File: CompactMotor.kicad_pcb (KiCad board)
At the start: 4 copper layers, 39.4 x 41.3 mm, 29 parts, among them J1 Conn_01x04_Male, U2 AMS1117-3.3

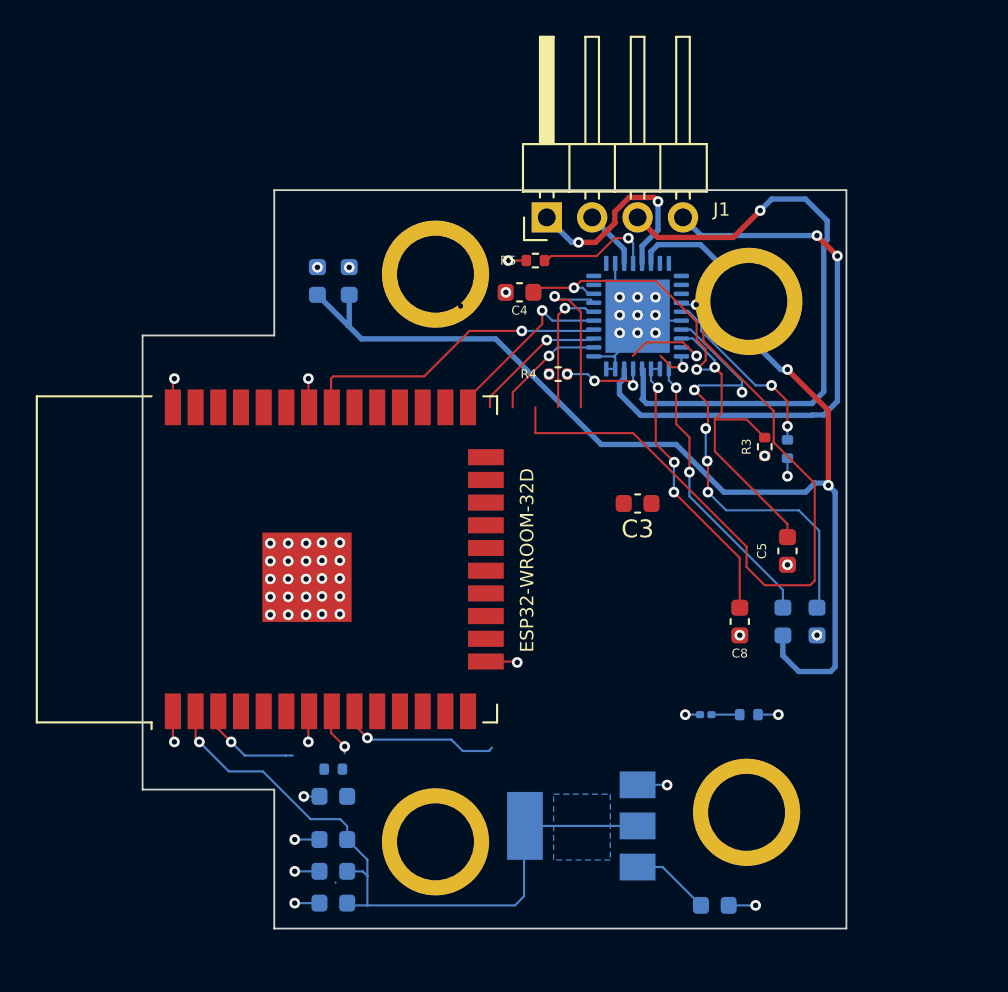
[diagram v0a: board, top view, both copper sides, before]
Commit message: Only trx-rx
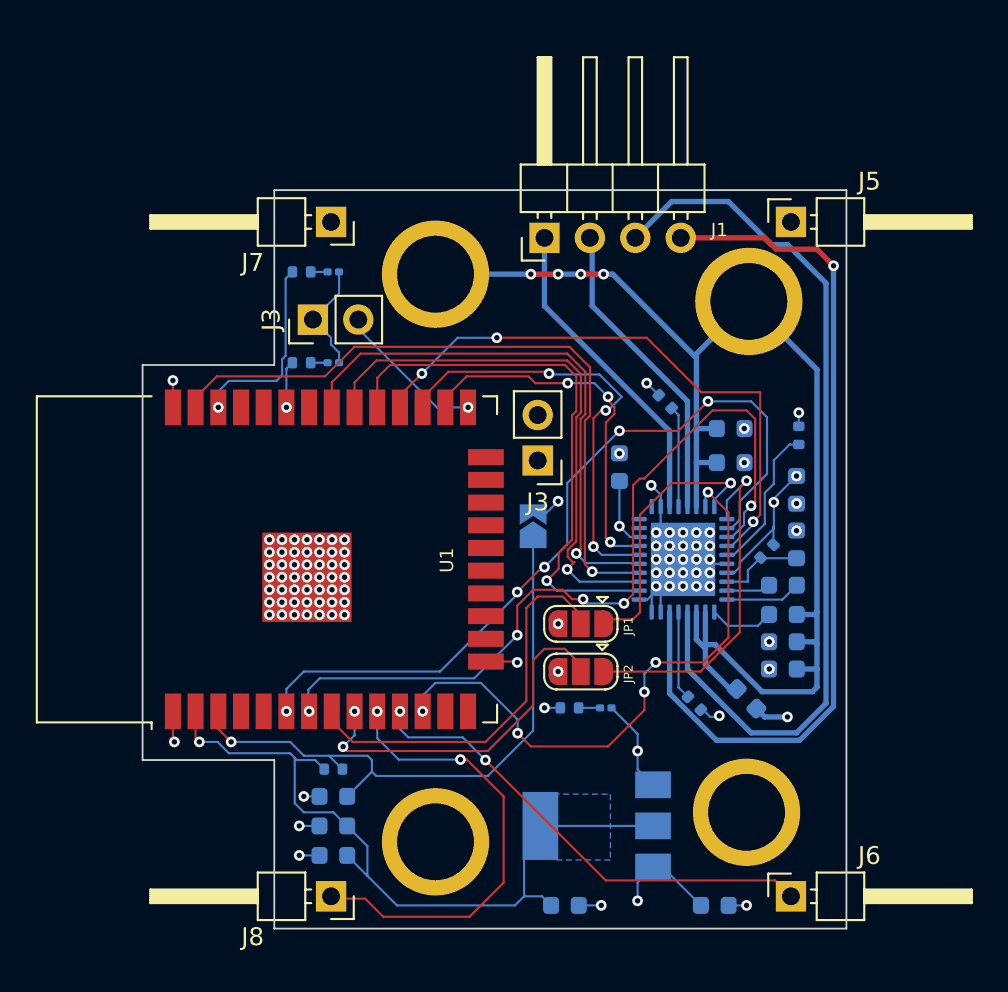
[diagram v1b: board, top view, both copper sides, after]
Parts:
- added C14: C100nF, Capacitor_SMD:C_0603_1608Metric, B.Cu at (28.4, 25.3)
- added C15: C1uF, Capacitor_SMD:C_0603_1608Metric, B.Cu at (28.4, 26.8)
- added D2: LED, LED_SMD:LED_0201_0603Metric, B.Cu at (3.30, 9.65)
- added D3: LED, LED_SMD:LED_0201_0603Metric, B.Cu at (3.30, 4.57)
- added J3: Conn_01x02_Female, Connector_PinHeader_2.54mm:PinHeader_1x02_P2.54mm_Vertical, F.Cu at (14.7, 15.1)
- added J3: Conn_01x02_Female, Connector_PinHeader_2.54mm:PinHeader_1x02_P2.54mm_Vertical, F.Cu at (2.16, 7.24)
- added J5: Conn_01x01_Male, Connector_PinHeader_2.54mm:PinHeader_1x01_P2.54mm_Horizontal, F.Cu at (28.9, 1.78)
- added J6: Conn_01x01_Male, Connector_PinHeader_2.54mm:PinHeader_1x01_P2.54mm_Horizontal, F.Cu at (28.9, 39.5)
- added J7: Conn_01x01_Male, Connector_PinHeader_2.54mm:PinHeader_1x01_P2.54mm_Horizontal, F.Cu at (3.17, 1.78)
- added J8: Conn_01x01_Male, Connector_PinHeader_2.54mm:PinHeader_1x01_P2.54mm_Horizontal, F.Cu at (3.17, 39.5)
- added JP1: SolderJumper_3_Open, Jumper:SolderJumper-3_P1.3mm_Open_RoundedPad1.0x1.5mm, F.Cu at (17.1, 24.3)
- added JP2: SolderJumper_3_Open, Jumper:SolderJumper-3_P1.3mm_Open_RoundedPad1.0x1.5mm, F.Cu at (17.1, 26.9)
- added JP3: SolderJumper_2_Open, Jumper:SolderJumper-2_P1.3mm_Open_TrianglePad1.0x1.5mm, B.Cu at (14.5, 18.8)
- added R7: R2k, Resistor_SMD:R_0402_1005Metric, B.Cu at (1.52, 9.65)
- added R8: R2k, Resistor_SMD:R_0402_1005Metric, B.Cu at (1.53, 4.57)
- C3, C4, C5, C8, R3, R4, R5: moved to B.Cu
- moved C13 24.5 mm to (25.5, 13.3), turned to 180 degrees
- moved C12 23.6 mm to (25.5, 15.2), turned to 0 degrees
- moved R4 19.9 mm to (23.5, 28.7), turned to 135 degrees
- moved U3 13.8 mm to (22.9, 20.6)
- moved C2 13.0 mm to (16.3, 40.0), turned to 0 degrees
- moved C4 11.3 mm to (19.3, 15.5), turned to -90 degrees
- moved R5 10.7 mm to (21.9, 11.8), turned to 135 degrees
- moved R1 10.0 mm to (16.5, 29.0), turned to 0 degrees
- moved C3 9.33 mm to (28.4, 22.1)
- moved C6 7.45 mm to (29.2, 16.8)
- moved R3 5.84 mm to (27.6, 20.2), turned to 45 degrees
- moved D1 5.60 mm to (18.5, 29.0), turned to 180 degrees
- moved C8 4.33 mm to (26.4, 28.4), turned to 135 degrees
- moved J1 1.15 mm to (15.1, 2.67)
- moved R2 0.99 mm to (29.3, 13.7), turned to -90 degrees
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- renumbered ESP32-WROOM-32D to U1, TMC2130 to U3
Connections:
- C4 pad 2: Net-(C4-Pad2) -> 5V0
- C5 pad 2: Net-(C4-Pad2) -> Net-(C5-Pad2)
- C8 pad 2: Net-(C8-Pad2) -> VM
- R3 pad 1: Net-(C4-Pad2) -> Net-(C5-Pad2)
- U1 pad 10: IO25 -> STALLPLUS
- U1 pad 11: IO26 -> STALLMINUS
- U1 pad 12: IO27 -> DC0
- U1 pad 25: SD0 -> IO0
- U1 pad 33: IO21 -> Net-(R7-Pad1)
- U1 pad 36: IO22 -> Net-(R8-Pad1)
- U1 pad 6: IO34 -> DIAG0
- U1 pad 7: IO35 -> DIAG1
- U1 pad 8: IO32 -> Net-(JP1-Pad2)
- U1 pad 9: IO33 -> Net-(JP2-Pad2)
- U3 pad 13: Net-(J1-Pad2) -> Net-(J1-Pad1)
- U3 pad 15: Net-(J1-Pad1) -> Net-(J1-Pad2)
- U3 pad 26: Net-(C4-Pad2) -> Net-(C5-Pad2)
- U3 pad 30: Net-(C8-Pad2) -> VM
- U3 pad 31: Net-(C8-Pad2) -> VM
- U3 pad 8: Net-(C4-Pad2) -> 5V0
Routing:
- net DIAG1: track 0.00 -> 45.5 mm, vias 0 -> 5
- net DIAG0: track 0.00 -> 44.5 mm, vias 0 -> 5
- net DC0: track 0.00 -> 33.4 mm, vias 0 -> 5
- net Net-(C4-Pad2): track 33.2 -> 0.00 mm, vias 3 -> 0
- net EN: track 5.77 -> 34.8 mm
- net STALLMINUS: track 0.00 -> 26.7 mm, vias 0 -> 2
- net STALLPLUS: track 0.00 -> 25.7 mm, vias 0 -> 2
- net CS: track 6.42 -> 30.9 mm
- net SCK: track 7.75 -> 30.8 mm
- net Net-(JP1-Pad2): track 0.00 -> 22.3 mm
- net MOSI: track 17.4 -> 38.6 mm
- net MISO: track 10.3 -> 30.8 mm
- net Net-(JP2-Pad2): track 0.00 -> 20.2 mm, vias 0 -> 2
- net DCIN_CFG5: track 0.00 -> 19.7 mm, vias 0 -> 1
- net GNDREF: track 25.9 -> 44.3 mm, vias 52 -> 97
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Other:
- outline, holes or cut-outs redrawn
- board text added: "STALL"
- board text added: "WIFI"
